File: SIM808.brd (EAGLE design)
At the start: 118.1 x 69.5 mm, 33 parts, among them IC1 LM1117S, IC2 MEGA32-A, J1 U.FL-R-SMT(01), Q1 CSM-7X-DU, SW1 1825910-2, SW2 1825910-2, U2 SN74ABT125PW, X1 SMA-142-0701-801/806, X2 5036_006_201_862

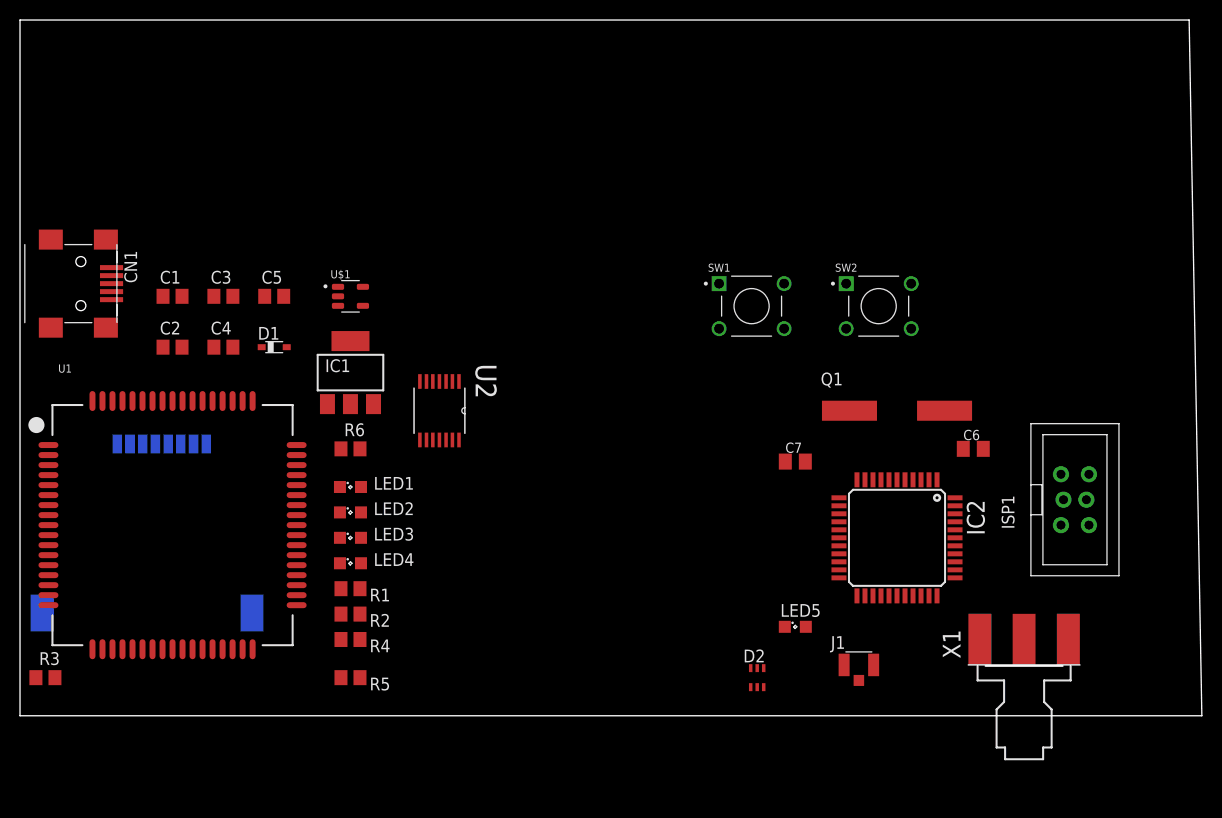
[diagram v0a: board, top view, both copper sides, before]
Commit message: routed design
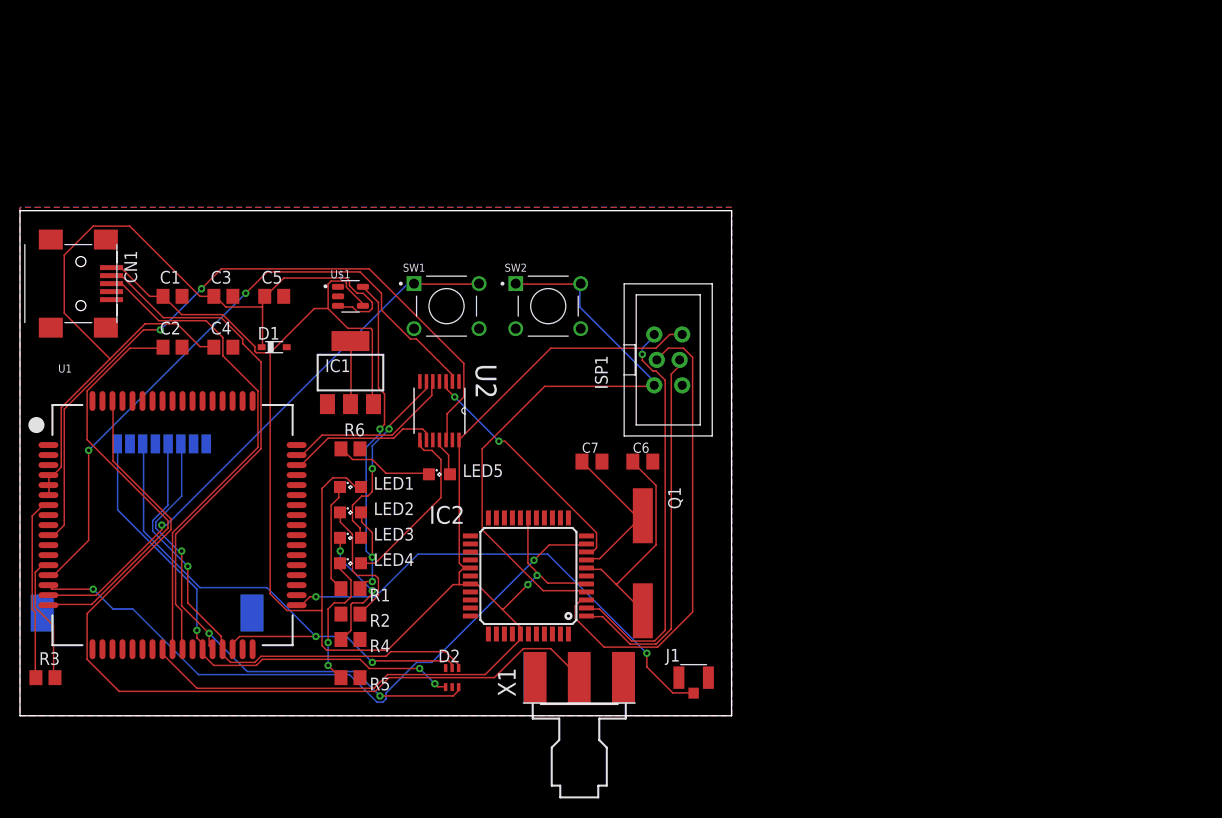
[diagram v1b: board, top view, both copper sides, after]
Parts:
- moved X1 44.6 mm to (55.9, 1.27)
- moved ISP1 43.0 mm to (64.8, 35.6)
- moved LED5 38.7 mm to (41.9, 24.1)
- moved IC2 37.0 mm to (50.8, 14.0), turned to 180 degrees
- moved C6 33.0 mm to (62.2, 25.4)
- moved SW2 33.0 mm to (49.5, 43.2)
- moved D2 30.5 mm to (43.2, 3.81)
- moved SW1 30.5 mm to (39.4, 43.2)
- moved Q1 29.6 mm to (62.2, 15.2), turned to 270 degrees
- moved C7 20.3 mm to (57.1, 25.4)
- moved J1 16.6 mm to (67.3, 3.81)
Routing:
- net +5V: track 0.00 -> 222.6 mm, vias 0 -> 2
- net VBAT: track 0.00 -> 88.4 mm
- net N$5: track 0.00 -> 85.2 mm
- net RING: track 0.00 -> 71.7 mm, vias 0 -> 2
- net GSM_RXD: track 0.00 -> 65.5 mm, vias 0 -> 2
- net GSM_TXD: track 0.00 -> 64.1 mm, vias 0 -> 2
- net RESET: track 0.00 -> 60.8 mm
- net GSM_RST: track 0.00 -> 56.2 mm, vias 0 -> 1
- net SIM_RST: track 0.00 -> 54.8 mm, vias 0 -> 2
- net SIM_DATA: track 0.00 -> 52.2 mm, vias 0 -> 3
- net USB_D-: track 0.00 -> 51.4 mm
- net 1.8V: track 0.00 -> 50.7 mm, vias 0 -> 3
- net SIM_CLK: track 0.00 -> 49.8 mm, vias 0 -> 1
- net USB_D+: track 0.00 -> 49.5 mm
- net N$6: track 0.00 -> 48.3 mm, vias 0 -> 2
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- added copper zone on layer 1, net GND
- added copper zone on layer 16, net GND
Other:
- board size 118.1 x 69.5 mm -> 71.1 x 50.5 mm
